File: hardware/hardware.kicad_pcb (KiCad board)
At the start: 2 copper layers, 100 x 100 mm, 138 parts, among them J1 Conn_01x04_Pin, J10 Conn_01x03, J11 AVR-ISP-6, J12 Conn_01x03, J13 Conn_01x03, J14 Conn_01x03, J2 Conn_01x04_Pin, J3 Conn_01x04_Pin, J4 Conn_01x04_Pin, J5 Conn_01x04_Pin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

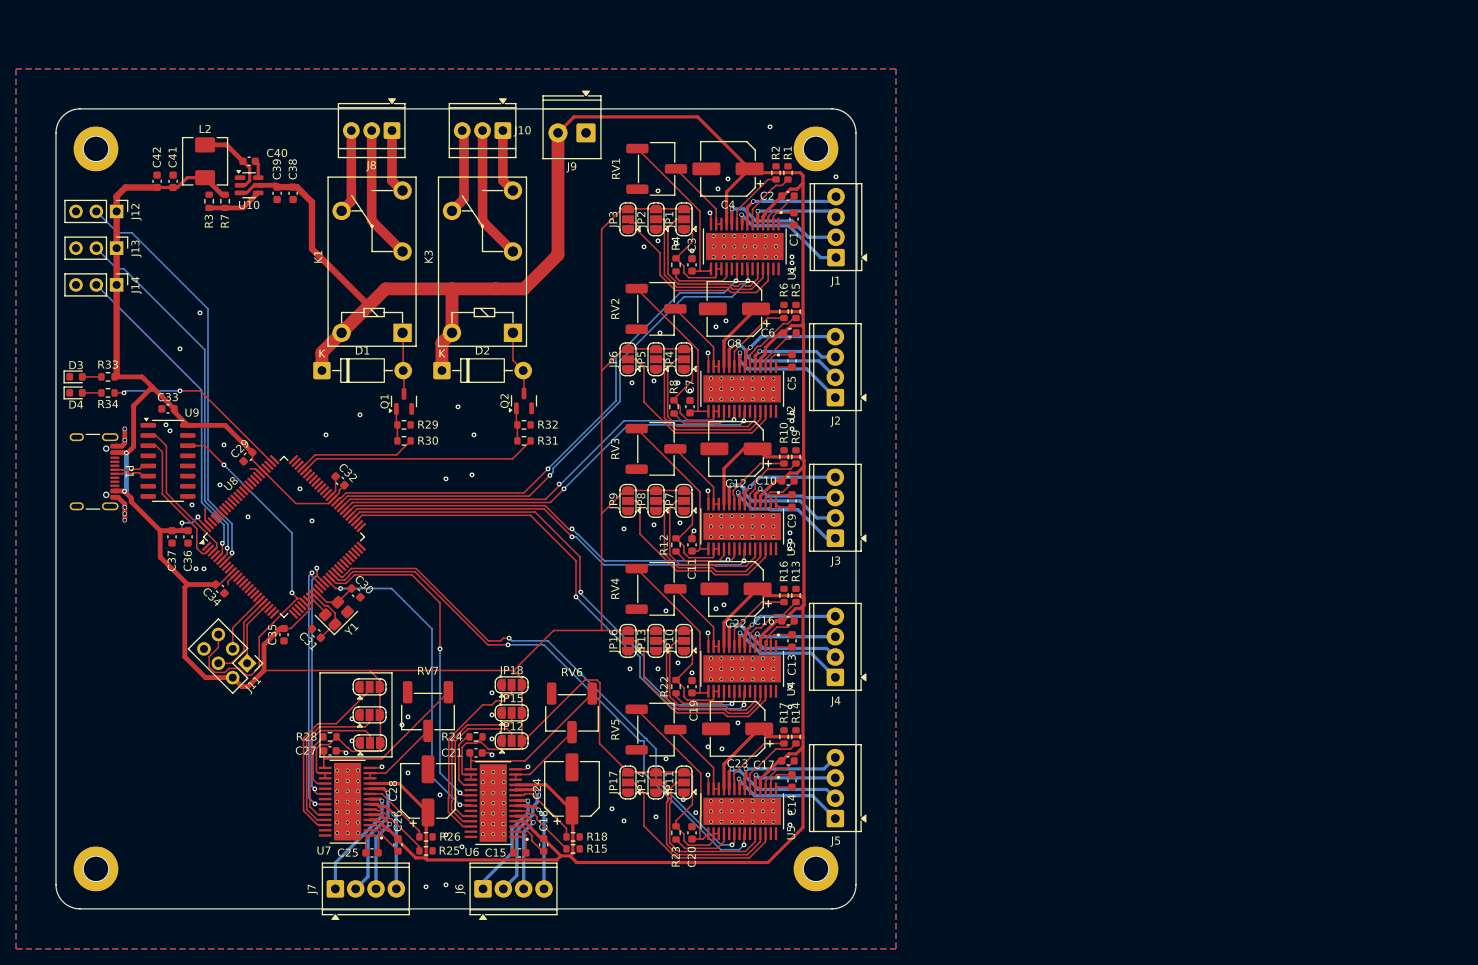
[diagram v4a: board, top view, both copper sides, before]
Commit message: wire current regulator
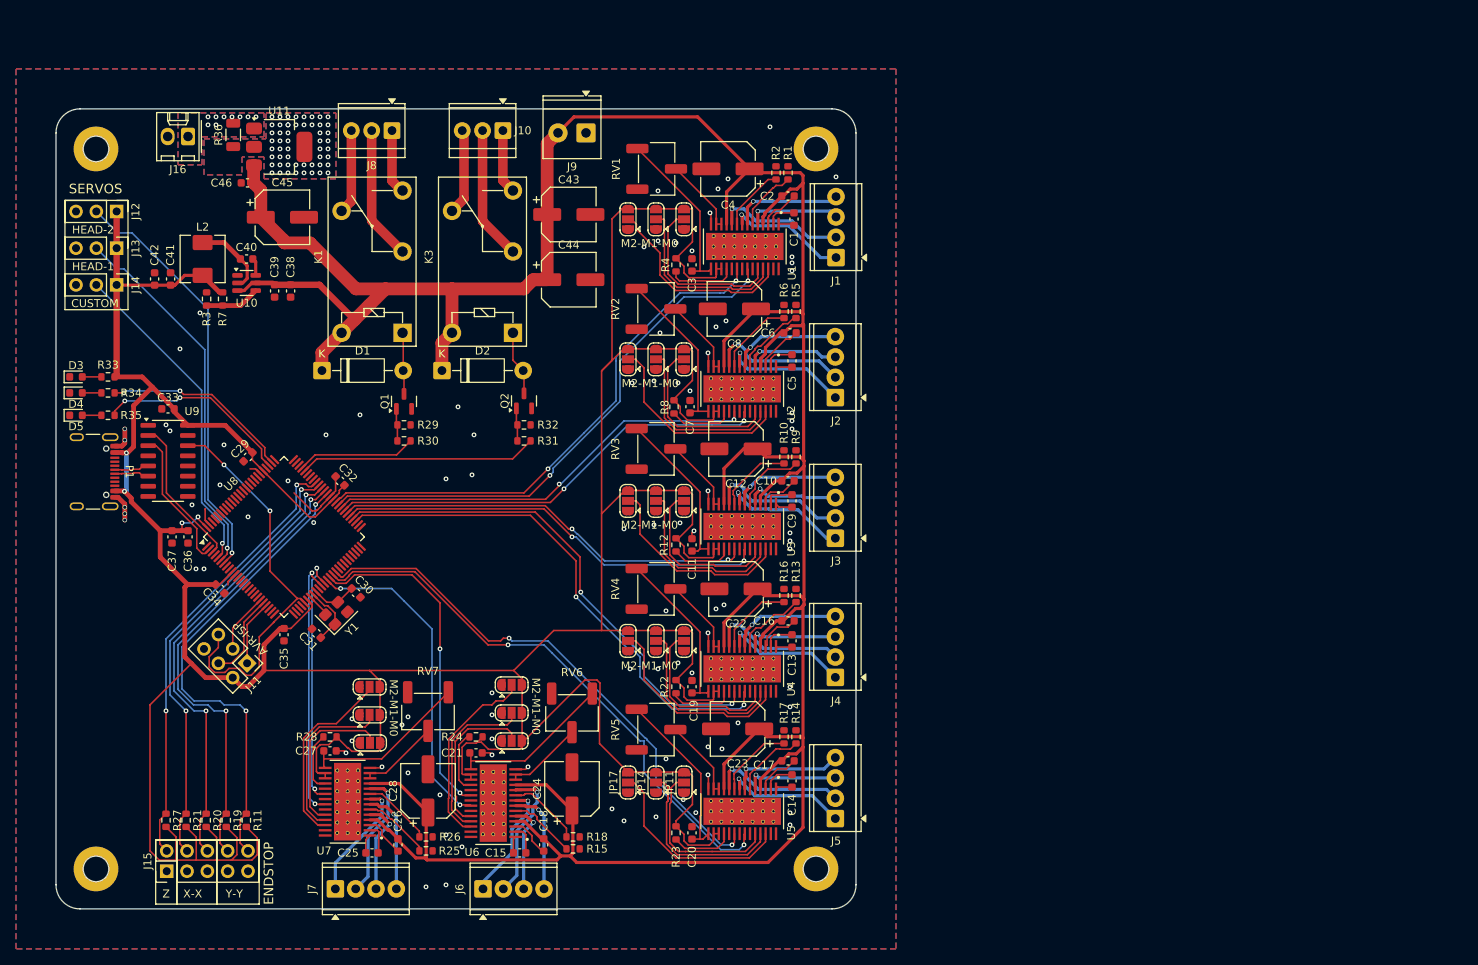
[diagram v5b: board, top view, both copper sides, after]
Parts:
- added C43: 100n, Capacitor_SMD:CP_Elec_6.3x5.7, F.Cu at (114.1, 63.2)
- added C44: 100n, Capacitor_SMD:CP_Elec_6.3x5.7, F.Cu at (114.1, 71.3)
- added C45: 100n, Capacitor_SMD:CP_Elec_6.3x5.7, F.Cu at (78.3, 63.5)
- added C46: 10pf, Capacitor_SMD:C_0603_1608Metric, F.Cu at (73.9, 59.2)
- added D5: LED, LED_SMD:LED_0603_1608Metric, F.Cu at (52.5, 88.3)
- added J15: Conn_02x05_Odd_Even, Connector_PinHeader_2.54mm:PinHeader_2x05_P2.54mm_Vertical, F.Cu at (63.8, 145.3)
- added J16: Conn_01x02, Connector_Molex:Molex_KK-254_AE-6410-02A_1x02_P2.54mm_Vertical, F.Cu at (66.5, 53.5)
- added R11: 10K, Resistor_SMD:R_0603_1608Metric, F.Cu at (73.8, 138.9)
- added R19: 10K, Resistor_SMD:R_0603_1608Metric, F.Cu at (71.3, 138.9)
- added R20: 10K, Resistor_SMD:R_0603_1608Metric, F.Cu at (68.8, 138.9)
- added R21: 10K, Resistor_SMD:R_0603_1608Metric, F.Cu at (66.3, 138.9)
- added R27: 10K, Resistor_SMD:R_0603_1608Metric, F.Cu at (63.8, 138.9)
- added R35: 1.1K, Resistor_SMD:R_0603_1608Metric, F.Cu at (56.5, 88.3)
- added R36: 12, Resistor_SMD:R_1206_3216Metric, F.Cu at (72.2, 53.2)
- added U11: LM317_SOT-223, Package_TO_SOT_SMD:SOT-223-3_TabPin2, F.Cu at (77.9, 54.8)
- moved C38 12.2 mm to (79.3, 72.8)
- moved C39 12.2 mm to (77.3, 72.8)
- moved C40 12.2 mm to (73.8, 68.8)
- moved C41 12.2 mm to (64.3, 71.3)
- moved C42 12.2 mm to (62.3, 71.3)
- moved L2 12.2 mm to (68.3, 68.8)
- moved R3 12.2 mm to (68.8, 73.8)
- moved R7 12.2 mm to (70.8, 73.8)
- moved U10 12.2 mm to (73.8, 71.8)
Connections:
- U8 pad 2: TX -> RX
- U8 pad 3: RX -> TX
- U8 pad 63: unconnected-(U8-PJ0-Pad63) -> END_STOP_1
- U8 pad 64: unconnected-(U8-PJ1-Pad64) -> END_STOP_2
- U8 pad 65: unconnected-(U8-PJ2-Pad65) -> END_STOP_3
- U8 pad 66: unconnected-(U8-PJ3-Pad66) -> END_STOP_4
- U8 pad 67: unconnected-(U8-PJ4-Pad67) -> END_STOP_5
- U8 pad 78: unconnected-(U8-PA0-Pad78) -> LED2
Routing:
- net +5V: track 457.2 -> 519.5 mm
- net END_STOP_1: track 0.00 -> 59.4 mm, vias 0 -> 2
- net END_STOP_2: track 0.00 -> 58.1 mm, vias 0 -> 2
- net END_STOP_3: track 0.00 -> 56.9 mm, vias 0 -> 2
- net END_STOP_5: track 0.00 -> 56.0 mm, vias 0 -> 2
- net END_STOP_4: track 0.00 -> 55.9 mm, vias 0 -> 2
- net LED2: track 0.00 -> 24.7 mm, vias 0 -> 2
- net +12V: track 410.4 -> 428.3 mm
- net GND: track 33.3 -> 39.6 mm
- net Net-(D5-A): track 0.00 -> 2.39 mm
- net LED1: track 23.5 -> 24.0 mm
- net Net-(U11-VO): vias 0 -> 53
- net Net-(J16-Pin_1): vias 0 -> 9
- added copper zone on B.Cu, net Net-(J16-Pin_1)
- added copper zone on F.Cu, net Net-(J16-Pin_1)
- added copper zone on B.Cu, net Net-(U11-VO)
- added copper zone on F.Cu, net Net-(U11-VO)
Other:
- board text added: "AVR-ISP"
- board text added: "CUSTOM"
- board text added: "ENDSTOP"
- board text added: "HEAD-1"
- board text added: "HEAD-2"
- board text added: "M2-M1-M0"
- board text added: "SERVOS"
- board text added: "X-X"
- board text added: "Y-Y"
- board text added: "Z"

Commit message: finish wiring
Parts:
- added G***: LOGO, R-logo:R-logo, F.Cu at (55.5, 106.2)
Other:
- board text added: "LED_CTL"
- board text added: "NC-COM-NO"
- board text added: "PUMP_CTL RELAYS"
- board text added: "X"
- board text added: "Y"

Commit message: add ftdi + buzzer + rst button
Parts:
- added BZ1: Buzzer, Buzzer_Beeper:Buzzer_TDK_PS1240P02BT_D12.2mm_H6.5mm, F.Cu at (58.2, 119.8)
- added J17: Conn_01x06, Connector_PinHeader_2.54mm:PinHeader_1x06_P2.54mm_Vertical, F.Cu at (53.0, 126.3)
- added R37: 10K, Resistor_SMD:R_0603_1608Metric, F.Cu at (57.8, 129.5)
- added RST: SW_Push, Button_Switch_SMD:SW_SPST_CK_RS282G05A3, F.Cu at (58.8, 135.2)
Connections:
- U8 pad 26: unconnected-(U8-PB7-Pad26) -> BUZZER
- U8 pad 8: unconnected-(U8-PE6-Pad8) -> BUZZER
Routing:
- net RST: track 49.8 -> 98.0 mm, vias 2 -> 3
- net RX: track 18.9 -> 52.4 mm, vias 0 -> 4
- net TX: track 18.0 -> 50.9 mm, vias 0 -> 2
- net BUZZER: track 0.00 -> 32.8 mm, vias 0 -> 3
- net +5V: track 519.5 -> 533.3 mm
- net GND: track 39.6 -> 42.0 mm, vias 94 -> 105
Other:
- board text added: "FTDI"
- board text added: "Pick O Matic"
